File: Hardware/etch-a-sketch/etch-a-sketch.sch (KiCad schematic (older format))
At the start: 32 parts, among them J1 USART, J2 Conn_02x05_Odd_Even, J3 OLED, SW1 Encoder 1, SW2 Encoder 2, U1 AMS1117-3.3, U2 STM32F401RET6

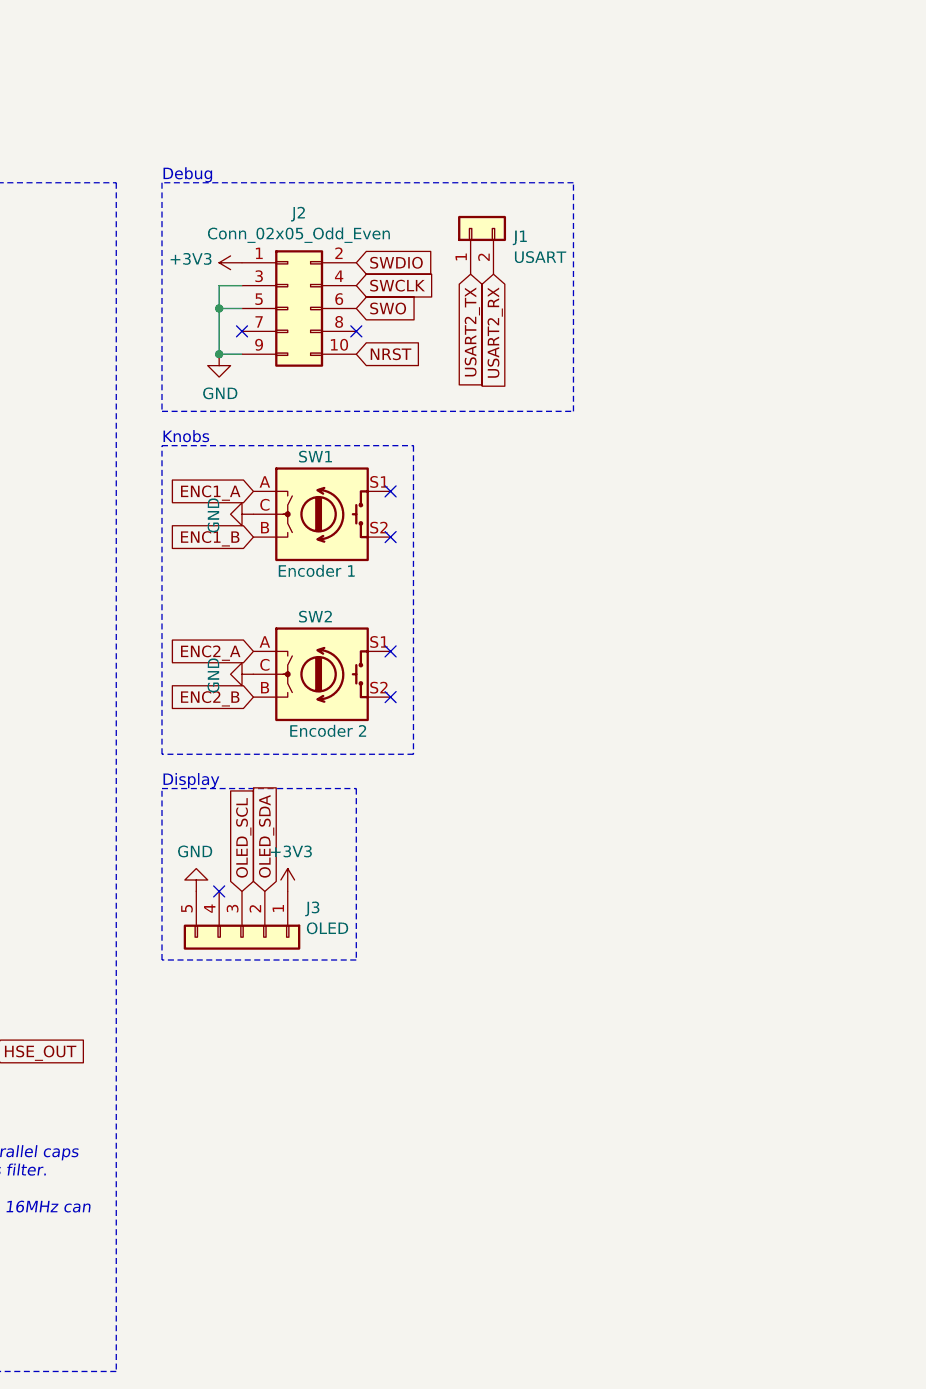
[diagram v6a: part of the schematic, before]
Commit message: feat: add micro USB connector
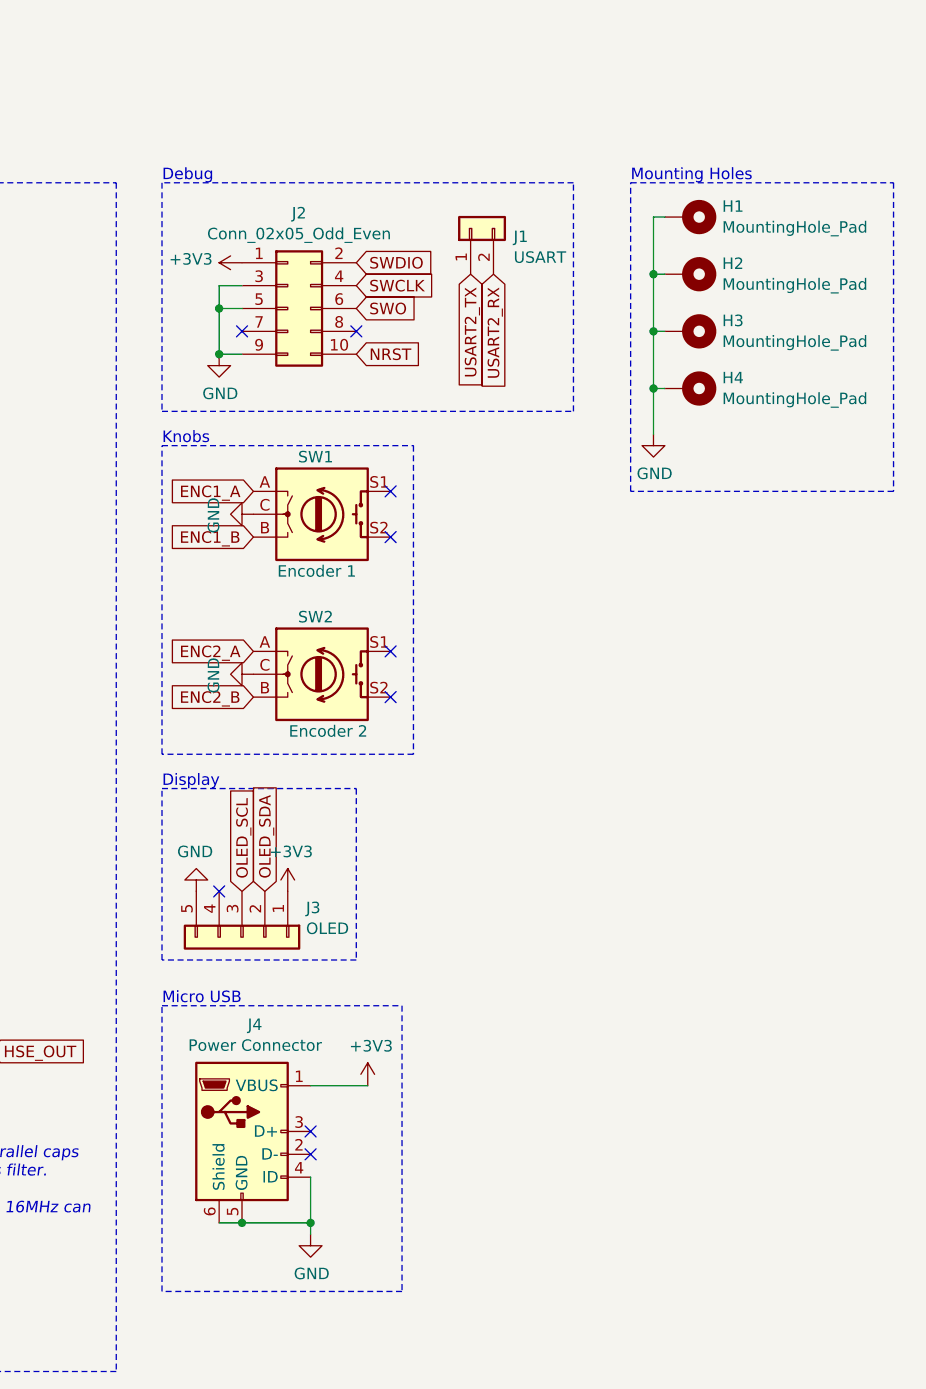
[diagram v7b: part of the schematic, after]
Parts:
- added H1, H2, H3, H4: MountingHole_Pad, symbol Mechanical:MountingHole_Pad
- added J4: Power Connector, symbol Connector:USB_B_Mini
- C1, C2: footprint (none) -> Capacitor_SMD:C_0805_2012Metric
- C10, C12, C13, C4, C5, C6, C7, C8, C9: footprint (none) -> Capacitor_SMD:C_0402_1005Metric
- C11, C3: footprint (none) -> Capacitor_SMD:C_0603_1608Metric
- D1: footprint (none) -> Diode_SMD:D_SOD-123
- D2, D3: footprint (none) -> LED_SMD:LED_0603_1608Metric
- F1: footprint (none) -> Fuse:Fuse_1206_3216Metric
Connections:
- net +3V3: now also J4.1 (VBUS)
- net GND: now also H1.1, H2.1, H3.1, H4.1, J4.4 (ID), J4.5 (GND), J4.6 (Shield)
- no-connect marks 42 -> 44
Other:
- note added: "Micro USB"
- note added: "Mounting Holes"
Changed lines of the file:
@@
 F 0 "F1" H 1400 1285 50  0000 C CNN
 F 1 "500mA" H 1400 1194 50  0000 C CNN
-F 2 "" H 1400 1100 50  0001 C CNN
+F 2 "Fuse:Fuse_1206_3216Metric" H 1400 1100 50  0001 C CNN
 F 3 "~" H 1400 1100 50  0001 C CNN
 	1    1400 1100
@@
 F 0 "D1" H 1050 895 50  0000 C CNN
 F 1 "B5819W" H 1050 986 50  0000 C CNN
-F 2 "" V 1050 1100 50  0001 C CNN
+F 2 "Diode_SMD:D_SOD-123" V 1050 1100 50  0001 C CNN
 F 3 "~" V 1050 1100 50  0001 C CNN
 	1    1050 1100
@@
 F 0 "C1" H 2092 1396 50  0000 L CNN
 F 1 "10uF" H 2092 1305 50  0000 L CNN
-F 2 "" H 2000 1350 50  0001 C CNN
+F 2 "Capacitor_SMD:C_0805_2012Metric" H 2000 1350 50  0001 C CNN
 F 3 "~" H 2000 1350 50  0001 C CNN
 	1    2000 1350
@@
 F 0 "C2" H 3092 1396 50  0000 L CNN
 F 1 "10uF" H 3092 1305 50  0000 L CNN
-F 2 "" H 3000 1350 50  0001 C CNN
+F 2 "Capacitor_SMD:C_0805_2012Metric" H 3000 1350 50  0001 C CNN
 F 3 "~" H 3000 1350 50  0001 C CNN
 	1    3000 1350
@@
 F 0 "C9" H 3892 2896 50  0000 L CNN
 F 1 "100nF" H 3892 2805 50  0000 L CNN
-F 2 "" H 3800 2850 50  0001 C CNN
+F 2 "Capacitor_SMD:C_0402_1005Metric" H 3800 2850 50  0001 C CNN
 F 3 "~" H 3800 2850 50  0001 C CNN
 	1    3800 2850
@@
 F 0 "C10" H 4342 2896 50  0000 L CNN
 F 1 "1uF" H 4342 2805 50  0000 L CNN
-F 2 "" H 4250 2850 50  0001 C CNN
+F 2 "Capacitor_SMD:C_0402_1005Metric" H 4250 2850 50  0001 C CNN
 F 3 "~" H 4250 2850 50  0001 C CNN
 	1    4250 2850
@@
 F 0 "C4" H 1242 2696 50  0000 L CNN
 F 1 "100nF" H 1242 2605 50  0000 L CNN
-F 2 "" H 1150 2650 50  0001 C CNN
+F 2 "Capacitor_SMD:C_0402_1005Metric" H 1150 2650 50  0001 C CNN
 F 3 "~" H 1150 2650 50  0001 C CNN
 	1    1150 2650
@@
 F 0 "C5" H 1642 2696 50  0000 L CNN
 F 1 "100nF" H 1642 2605 50  0000 L CNN
-F 2 "" H 1550 2650 50  0001 C CNN
+F 2 "Capacitor_SMD:C_0402_1005Metric" H 1550 2650 50  0001 C CNN
 F 3 "~" H 1550 2650 50  0001 C CNN
 	1    1550 2650
@@
 F 0 "C6" H 2042 2696 50  0000 L CNN
 F 1 "100nF" H 2042 2605 50  0000 L CNN
-F 2 "" H 1950 2650 50  0001 C CNN
+F 2 "Capacitor_SMD:C_0402_1005Metric" H 1950 2650 50  0001 C CNN
 F 3 "~" H 1950 2650 50  0001 C CNN
 	1    1950 2650
@@
 F 0 "C7" H 2442 2696 50  0000 L CNN
 F 1 "100nF" H 2442 2605 50  0000 L CNN
-F 2 "" H 2350 2650 50  0001 C CNN
+F 2 "Capacitor_SMD:C_0402_1005Metric" H 2350 2650 50  0001 C CNN
 F 3 "~" H 2350 2650 50  0001 C CNN
 	1    2350 2650
@@
 F 0 "C8" H 2842 2696 50  0000 L CNN
 F 1 "100nF" H 2842 2605 50  0000 L CNN
-F 2 "" H 2750 2650 50  0001 C CNN
+F 2 "Capacitor_SMD:C_0402_1005Metric" H 2750 2650 50  0001 C CNN
 F 3 "~" H 2750 2650 50  0001 C CNN
 	1    2750 2650
@@
 F 0 "C3" H 842 2696 50  0000 L CNN
 F 1 "10uF" H 842 2605 50  0000 L CNN
-F 2 "" H 750 2650 50  0001 C CNN
+F 2 "Capacitor_SMD:C_0603_1608Metric" H 750 2650 50  0001 C CNN
 F 3 "~" H 750 2650 50  0001 C CNN
 	1    750  2650
@@
 F 0 "C13" H 4342 6246 50  0000 L CNN
 F 1 "12pF" H 4342 6155 50  0000 L CNN
-F 2 "" H 4250 6200 50  0001 C CNN
+F 2 "Capacitor_SMD:C_0402_1005Metric" H 4250 6200 50  0001 C CNN
 F 3 "~" H 4250 6200 50  0001 C CNN
 	1    4250 6200
@@
 F 0 "C12" H 3550 6250 50  0000 L CNN
 F 1 "12pF" H 3450 6150 50  0000 L CNN
-F 2 "" H 3750 6200 50  0001 C CNN
+F 2 "Capacitor_SMD:C_0402_1005Metric" H 3750 6200 50  0001 C CNN
 F 3 "~" H 3750 6200 50  0001 C CNN
 	1    3750 6200
@@
 F 0 "D3" H 2900 6550 50  0000 C CNN
 F 1 "Red" H 2900 6650 50  0000 C CNN
-F 2 "" V 3100 6600 50  0001 C CNN
+F 2 "LED_SMD:LED_0603_1608Metric" V 3100 6600 50  0001 C CNN
 F 3 "~" V 3100 6600 50  0001 C CNN
 	1    3100 6600
@@
 F 0 "D2" H 3350 895 50  0000 C CNN
 F 1 "Red" H 3350 986 50  0000 C CNN
-F 2 "" V 3350 1100 50  0001 C CNN
+F 2 "LED_SMD:LED_0603_1608Metric" V 3350 1100 50  0001 C CNN
 F 3 "~" V 3350 1100 50  0001 C CNN
 	1    3350 1100
@@
 F 0 "C11" H 892 4346 50  0000 L CNN
 F 1 "4.7uF" H 892 4255 50  0000 L CNN
-F 2 "" H 800 4300 50  0001 C CNN
+F 2 "Capacitor_SMD:C_0603_1608Metric" H 800 4300 50  0001 C CNN
 F 3 "~" H 800 4300 50  0001 C CNN
 	1    800  4300
@@
 Text GLabel 6850 2600 3    50   Input ~ 0
 USART2_RX
+$Comp
+L Mechanical:MountingHole_Pad H2
+U 1 1 5ED69F9D
+P 7700 2600
+F 0 "H2" V 7654 2750 50  0000 L CNN
+F 1 "MountingHole_Pad" V 7745 2750 50  0000 L CNN
+F 2 "" H 7700 2600 50  0001 C CNN
+F 3 "~" H 7700 2600 50  0001 C CNN
+	1    7700 2600
+	0    1    1    0
+$EndComp
+$Comp
+L Mechanical:MountingHole_Pad H3
+U 1 1 5ED6A288
+P 7700 2850
+F 0 "H3" V 7654 3000 50  0000 L CNN
+F 1 "MountingHole_Pad" V 7745 3000 50  0000 L CNN
+F 2 "" H 7700 2850 50  0001 C CNN
+F 3 "~" H 7700 2850 50  0001 C CNN
+	1    7700 2850
+	0    1    1    0
+$EndComp
+$Comp
+L Mechanical:MountingHole_Pad H4
+U 1 1 5ED6AB54
+P 7700 3100
+F 0 "H4" V 7654 3250 50  0000 L CNN
+F 1 "MountingHole_Pad" V 7745 3250 50  0000 L CNN
+F 2 "" H 7700 3100 50  0001 C CNN
+F 3 "~" H 7700 3100 50  0001 C CNN
+	1    7700 3100
+	0    1    1    0
+$EndComp
+$Comp
+L power:GND #PWR0101
+U 1 1 5ED73CC9
+P 7550 3300
+F 0 "#PWR0101" H 7550 3050 50  0001 C CNN
+F 1 "GND" H 7555 3127 50  0000 C CNN
+F 2 "" H 7550 3300 50  0001 C CNN
+F 3 "" H 7550 3300 50  0001 C CNN
+	1    7550 3300
+	1    0    0    -1
+$EndComp
+Wire Wire Line
+	7600 3100 7550 3100
+Wire Wire Line
+	7550 3100 7550 3300
+Wire Wire Line
+	7600 2850 7550 2850
+Wire Wire Line
+	7550 2850 7550 3100
+Connection ~ 7550 3100
+Wire Wire Line
+	7600 2600 7550 2600
+Wire Wire Line
+	7550 2600 7550 2850
+Connection ~ 7550 2850
+Connection ~ 7550 2600
+Wire Wire Line
+	7550 2350 7550 2600
+Wire Wire Line
+	7600 2350 7550 2350
+$Comp
+L Mechanical:MountingHole_Pad H1
+U 1 1 5ED6970A
+P 7700 2350
+F 0 "H1" V 7654 2500 50  0000 L CNN
+F 1 "MountingHole_Pad" V 7745 2500 50  0000 L CNN
+F 2 "" H 7700 2350 50  0001 C CNN
+F 3 "~" H 7700 2350 50  0001 C CNN
+	1    7700 2350
+	0    1    1    0
+$EndComp
+Wire Notes Line
+	8600 2200 8600 3550
+Wire Notes Line
+	8600 3550 7450 3550
+Wire Notes Line
+	7450 3550 7450 2200
+Wire Notes Line
+	7450 2200 8600 2200
+Text Notes 7450 2200 0    50   ~ 0
+Mounting Holes
+$Comp
+L Connector:USB_B_Mini J4
+U 1 1 5EDAFB76
+P 5750 6350
+F 0 "J4" H 5807 6817 50  0000 C CNN
+F 1 "Power Connector" H 5807 6726 50  0000 C CNN
+F 2 "" H 5900 6300 50  0001 C CNN
+F 3 "~" H 5900 6300 50  0001 C CNN
+	1    5750 6350
+	1    0    0    -1
+$EndComp
+$Comp
+L power:+3V3 #PWR024
+U 1 1 5EDB2618
+P 6300 6150
+F 0 "#PWR024" H 6300 6000 50  0001 C CNN
+F 1 "+3V3" H 6315 6323 50  0000 C CNN
+F 2 "" H 6300 6150 50  0001 C CNN
+F 3 "" H 6300 6150 50  0001 C CNN
+	1    6300 6150
+	1    0    0    -1
+$EndComp
+Wire Wire Line
+	6050 6150 6300 6150
+NoConn ~ 6050 6350
+NoConn ~ 6050 6450
+$Comp
+L power:GND #PWR025
+U 1 1 5EDBF07A
+P 6050 6800
+F 0 "#PWR025" H 6050 6550 50  0001 C CNN
+F 1 "GND" H 6055 6627 50  0000 C CNN
+F 2 "" H 6050 6800 50  0001 C CNN
+F 3 "" H 6050 6800 50  0001 C CNN
+	1    6050 6800
+	1    0    0    -1
+$EndComp
+Wire Wire Line
+	5750 6750 6050 6750
+Wire Wire Line
+	6050 6750 6050 6800
+Wire Wire Line
+	6050 6550 6050 6750
+Connection ~ 6050 6750
+Wire Wire Line
+	5650 6750 5750 6750
+Connection ~ 5750 6750
+Wire Notes Line
+	5400 5800 6450 5800
+Wire Notes Line
+	6450 5800 6450 7050
+Wire Notes Line
+	6450 7050 5400 7050
+Wire Notes Line
+	5400 7050 5400 5800
+Text Notes 5400 5800 0    50   ~ 0
+Micro USB
 $EndSCHEMATC
